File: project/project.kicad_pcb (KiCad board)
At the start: 6 copper layers, 66 x 16 mm, 114 parts, among them J1 2x5, J2 RJ45_Shielded, J3 USB_C_Receptacle_USB2.0, SW1 MOD, U1 GX101, U2 MAX13487E, U3 XL1050, U4 DP9900, U5 ME6211C33, U6 W5500, U7 USBLC6-2SC6, U8 esp32-C3FH4X, Y1 25MHz, Y2 40MHz

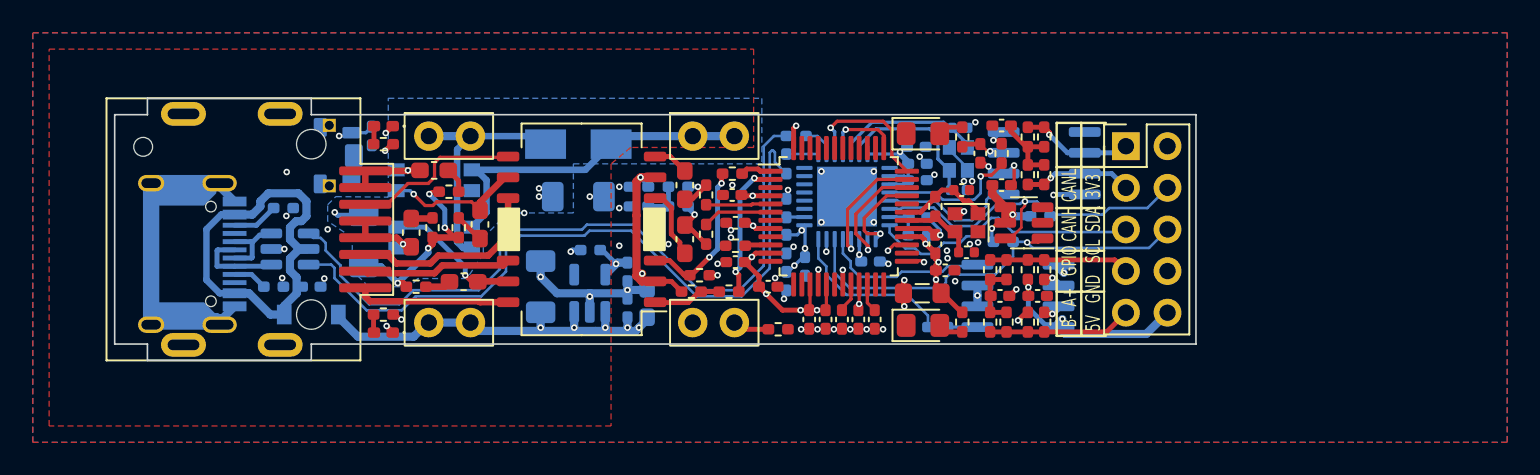
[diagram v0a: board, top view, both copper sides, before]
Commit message: enlarging vias to 0.45mm
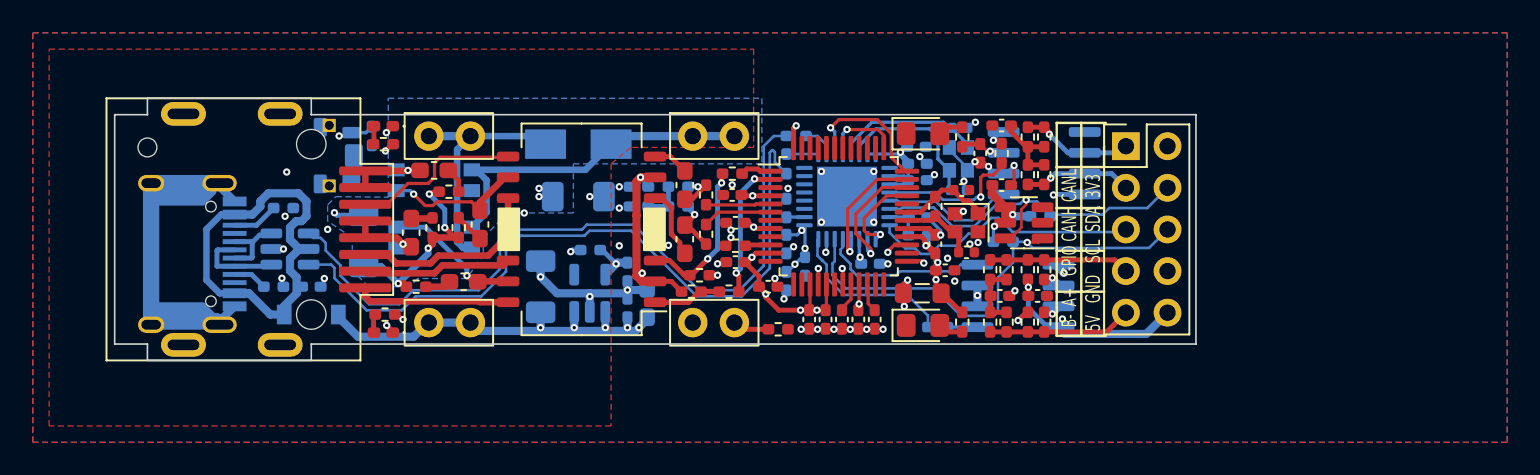
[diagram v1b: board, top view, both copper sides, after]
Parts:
- moved REF** 0.27 mm to (120.3, 78.0)
- moved C42 0.14 mm to (164.4, 85.1)
- moved R27 0.10 mm to (134.8, 88.2)
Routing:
- net SCL: track 26.4 -> 29.2 mm
- net /ETH/ACT_LED: track 35.0 -> 35.9 mm
- net /ETH/SPD_LED: track 53.0 -> 53.6 mm
- net /ETH/MISO: track 6.97 -> 7.55 mm
- net GND: vias 57 -> 56
